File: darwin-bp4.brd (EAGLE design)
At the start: 95 x 128 mm, 21 parts, among them U1 MCP23008, U2 TCA9548A, U3 LP5012

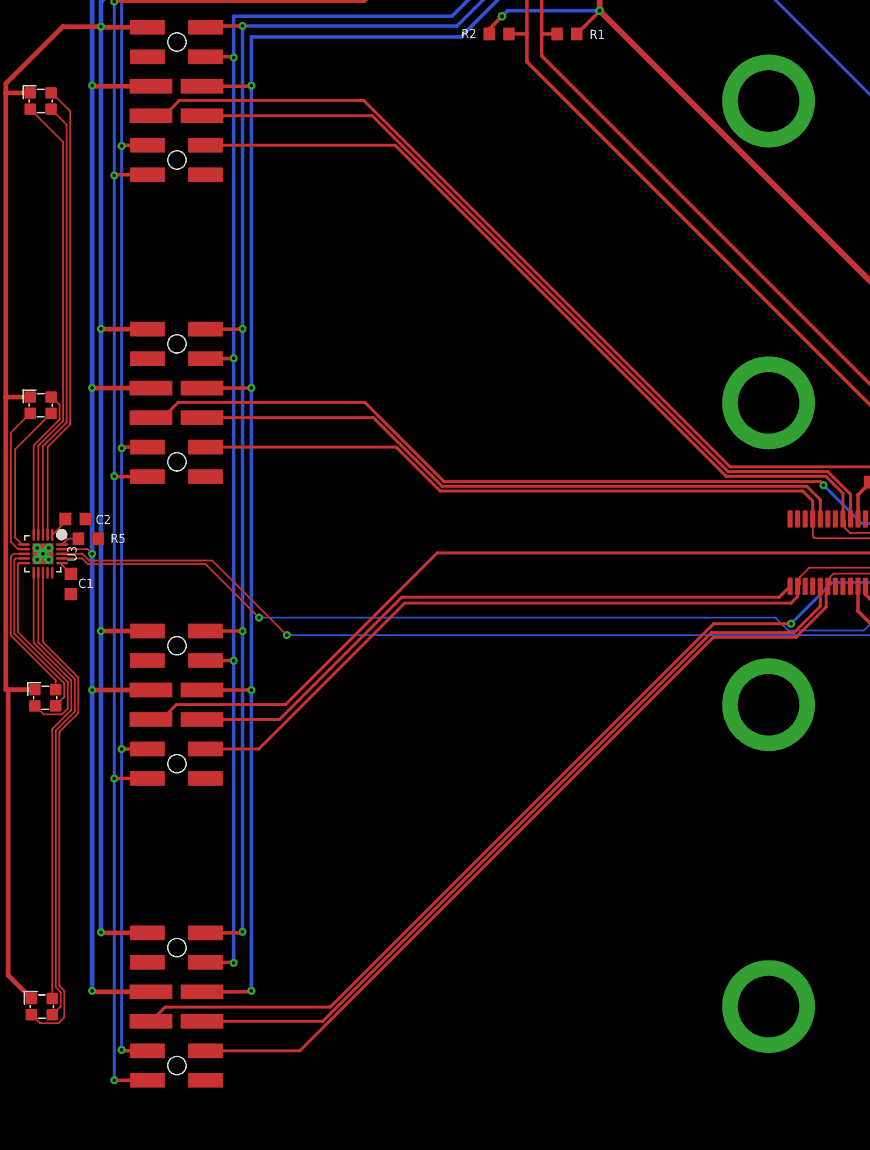
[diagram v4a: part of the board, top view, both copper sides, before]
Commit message: Fixed power to LED controller, added pulldowns on hot swap detection pins, adjusted standoff holes.
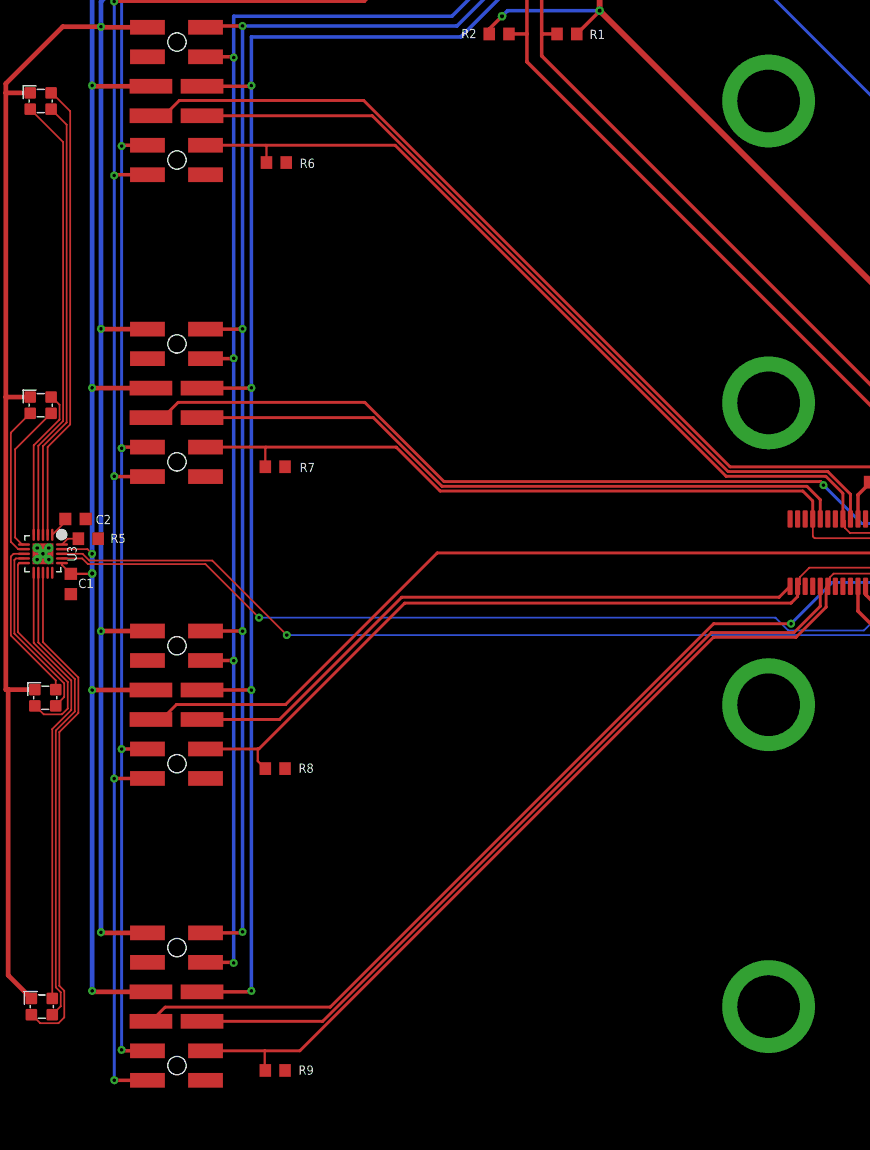
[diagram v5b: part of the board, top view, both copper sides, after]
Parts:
- added R6, R7, R8, R9: 100k, rcl:R0603
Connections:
- net GND: now also R6.2, R7.2, R8.2, R9.2
- net SC0: now also R6.1
- net SC1: now also R7.1
- net SC2: now also R8.1
- net SC3: now also R9.1
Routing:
- net SC2: track 69.5 -> 71.5 mm
- net 3V3: track 292.7 -> 294.6 mm, vias 10 -> 11
- net SC3: track 81.8 -> 83.5 mm
- net SC1: track 67.2 -> 68.9 mm
- net SC0: track 79.0 -> 80.5 mm
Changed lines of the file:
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@@
 <?xml version="1.0" encoding="utf-8"?>
 <!DOCTYPE eagle SYSTEM "eagle.dtd">
-<eagle version="9.5.0">
+<eagle version="9.5.2">
 <drawing>
 <settings>
@@
 <setting verticaltext="up"/>
 </settings>
-<grid distance="0.1" unitdist="mm" unit="mm" style="lines" multiple="1" display="yes" altdistance="0.1" altunitdist="mm" altunit="mm"/>
+<grid distance="0.5" unitdist="mm" unit="mm" style="lines" multiple="1" display="yes" altdistance="0.1" altunitdist="mm" altunit="mm"/>
 <layers>
 <layer number="1" name="Top" color="4" fill="1" visible="yes" active="yes"/>
@@
 <layer number="29" name="tStop" color="7" fill="3" visible="no" active="yes"/>
 <layer number="30" name="bStop" color="7" fill="6" visible="no" active="yes"/>
-<layer number="31" name="tCream" color="7" fill="4" visible="no" active="yes"/>
+<layer number="31" name="tCream" color="7" fill="4" visible="yes" active="yes"/>
 <layer number="32" name="bCream" color="7" fill="5" visible="no" active="yes"/>
 <layer number="33" name="tFinish" color="6" fill="3" visible="yes" active="yes"/>
@@
 <wire x1="70" y1="112.5" x2="70" y2="93.5" width="0.1524" layer="48"/>
 <hole x="67.7192" y="121.4724" drill="2.7"/>
+<wire x1="68.6" y1="106.3" x2="69.9" y2="100" width="1" layer="31" curve="-153.247402"/>
+<wire x1="68.4" y1="99.7" x2="67.1" y2="106" width="1" layer="31" curve="-153.247402"/>
+<wire x1="68.6" y1="80.3" x2="69.9" y2="74" width="1" layer="31" curve="-153.247402"/>
+<wire x1="68.4" y1="73.7" x2="67.1" y2="80" width="1" layer="31" curve="-153.247402"/>
+<wire x1="68.6" y1="54.3" x2="69.9" y2="48" width="1" layer="31" curve="-153.247402"/>
+<wire x1="68.4" y1="47.7" x2="67.1" y2="54" width="1" layer="31" curve="-153.247402"/>
+<wire x1="68.6" y1="28.3" x2="69.9" y2="22" width="1" layer="31" curve="-153.247402"/>
+<wire x1="68.4" y1="21.7" x2="67.1" y2="28" width="1" layer="31" curve="-153.247402"/>
 </plain>
 <attributes>
@@
 <element name="U$3" library="Conservify" library_urn="urn:adsk.eagle:library:11839183" package="2MMPLCC4" package3d_urn="urn:adsk.eagle:package:14540839/1" value="CLMVC-FKC-CGJJM569ABB7A343" x="6.2" y="51.6" smashed="yes" rot="R180"/>
 <element name="U$4" library="Conservify" library_urn="urn:adsk.eagle:library:11839183" package="2MMPLCC4" package3d_urn="urn:adsk.eagle:package:14540839/1" value="CLMVC-FKC-CGJJM569ABB7A343" x="5.9" y="25" smashed="yes" rot="R180"/>
+<element name="R6" library="rcl" library_urn="urn:adsk.eagle:library:334" package="R0603" package3d_urn="urn:adsk.eagle:package:23555/3" value="100k" x="26.1" y="97.7" smashed="yes">
+<attribute name="NAME" x="28.765" y="97.635" size="0.8" layer="25" rot="R180" align="center"/>
+<attribute name="SPICEPREFIX" value="R" x="26.1" y="97.7" size="0.799996875" layer="27" ratio="20" display="off"/>
+<attribute name="VALUE" x="25.465" y="95.795" size="1.27" layer="27"/>
+</element>
+<element name="R7" library="rcl" library_urn="urn:adsk.eagle:library:334" package="R0603" package3d_urn="urn:adsk.eagle:package:23555/3" value="100k" x="26" y="71.5" smashed="yes">
+<attribute name="NAME" x="28.765" y="71.435" size="0.8" layer="25" rot="R180" align="center"/>
+<attribute name="SPICEPREFIX" value="R" x="26" y="71.5" size="0.799996875" layer="27" ratio="20" display="off"/>
+<attribute name="VALUE" x="25.365" y="69.595" size="1.27" layer="27"/>
+</element>
+<element name="R8" library="rcl" library_urn="urn:adsk.eagle:library:334" package="R0603" package3d_urn="urn:adsk.eagle:package:23555/3" value="100k" x="26" y="45.5" smashed="yes">
+<attribute name="NAME" x="28.665" y="45.535" size="0.8" layer="25" rot="R180" align="center"/>
+<attribute name="SPICEPREFIX" value="R" x="26" y="45.5" size="0.799996875" layer="27" ratio="20" display="off"/>
+<attribute name="VALUE" x="25.365" y="43.595" size="1.27" layer="27"/>
+</element>
+<element name="R9" library="rcl" library_urn="urn:adsk.eagle:library:334" package="R0603" package3d_urn="urn:adsk.eagle:package:23555/3" value="100k" x="26" y="19.5" smashed="yes">
+<attribute name="NAME" x="28.665" y="19.535" size="0.8" layer="25" rot="R180" align="center"/>
+<attribute name="SPICEPREFIX" value="R" x="26" y="19.5" size="0.799996875" layer="27" ratio="20" display="off"/>
+<attribute name="VALUE" x="25.365" y="17.595" size="1.27" layer="27"/>
+</element>
 </elements>
 <signals>
@@
 <wire x1="10.234" y1="104.331" x2="10.234" y2="78.296" width="0.4064" layer="16"/>
 <wire x1="10.234" y1="78.296" x2="10.234" y2="64" width="0.4064" layer="16"/>
-<wire x1="10.234" y1="64" x2="10.234" y2="52.261" width="0.4064" layer="16"/>
+<wire x1="10.234" y1="64" x2="10.234" y2="62.3" width="0.4064" layer="16"/>
+<wire x1="10.234" y1="62.3" x2="10.234" y2="52.261" width="0.4064" layer="16"/>
 <wire x1="10.234" y1="52.261" x2="10.234" y2="26.353" width="0.4064" layer="16"/>
 <wire x1="15.3" y1="104.27" x2="10.295" y2="104.27" width="0.4064" layer="1"/>
@@
 <wire x1="79.5" y1="58.784" x2="79.708" y2="58.992" width="0.1524" layer="1"/>
 <wire x1="81" y1="57.875" x2="81" y2="58.992" width="0.1524" layer="1"/>
-<wire x1="7.6346" y1="64.4" x2="7.6346" y2="63.2" width="0" layer="19" extent="1-1"/>
+<wire x1="8.4" y1="62.275" x2="10.209" y2="62.275" width="0.2032" layer="1"/>
+<wire x1="10.209" y1="62.275" x2="10.234" y2="62.3" width="0.1524" layer="1"/>
+<via x="10.234" y="62.3" extent="1-16" drill="0.35"/>
 </signal>
 <signal name="GND">
@@
 <vertex x="0" y="0"/>
 </polygon>
-<via x="68.5" y="103" extent="1-16" drill="5.3" diameter="8"/>
-<via x="68.5" y="77" extent="1-16" drill="5.3" diameter="8"/>
-<via x="68.5" y="51" extent="1-16" drill="5.3" diameter="8"/>
-<via x="68.5" y="25" extent="1-16" drill="5.3" diameter="8"/>
+<via x="68.5" y="103" extent="1-16" drill="5.4" diameter="8"/>
+<via x="68.5" y="77" extent="1-16" drill="5.4" diameter="8"/>
+<via x="68.5" y="51" extent="1-16" drill="5.4" diameter="8"/>
+<via x="68.5" y="25" extent="1-16" drill="5.4" diameter="8"/>
 <contactref element="C2" pad="1"/>
 <contactref element="R5" pad="2"/>
@@
 <vertex x="0" y="0"/>
 </polygon>
+<contactref element="R6" pad="2"/>
+<contactref element="R7" pad="2"/>
+<contactref element="R8" pad="2"/>
+<contactref element="R9" pad="2"/>
 <wire x1="6.5" y1="64.5" x2="6" y2="64" width="0" layer="19" extent="1-1"/>
 </signal>
@@
 <contactref element="U2" pad="PIN5"/>
 <contactref element="SLOT1" pad="8"/>
-<wire x1="20" y1="99.19" x2="36.33" y2="99.19" width="0.254" layer="1"/>
+<wire x1="20" y1="99.19" x2="25.2" y2="99.19" width="0.254" layer="1"/>
+<wire x1="25.2" y1="99.19" x2="36.33" y2="99.19" width="0.254" layer="1"/>
 <wire x1="64.844" y1="70.676" x2="73.4292" y2="70.676" width="0.254" layer="1"/>
 <wire x1="74.9" y1="67" x2="74.9" y2="69.2052" width="0.254" layer="1"/>
@@
 <wire x1="78.816" y1="67.884" x2="82.176" y2="67.884" width="0.1524" layer="1"/>
 <wire x1="75.50523125" y1="65.7992" x2="77.54476875" y2="65.7992" width="0.1524" layer="1"/>
+<contactref element="R6" pad="1"/>
+<wire x1="25.25" y1="97.7" x2="25.25" y2="99.14" width="0.2" layer="1"/>
+<wire x1="25.25" y1="99.14" x2="25.2" y2="99.19" width="0.2" layer="1"/>
 </signal>
 <signal name="SC1">
 <contactref element="U2" pad="PIN9"/>
 <contactref element="SLOT2" pad="8"/>
-<wire x1="20" y1="73.19" x2="36.422" y2="73.19" width="0.254" layer="1"/>
+<wire x1="20" y1="73.19" x2="25.2" y2="73.19" width="0.254" layer="1"/>
+<wire x1="25.2" y1="73.19" x2="36.422" y2="73.19" width="0.254" layer="1"/>
 <wire x1="72.3" y1="68.554" x2="72.3" y2="67" width="0.254" layer="1"/>
 <wire x1="36.422" y1="73.19" x2="40.206" y2="69.406" width="0.254" layer="1"/>
@@
 <wire x1="72.3116" y1="65.4944" x2="72.462" y2="65.344" width="0.1524" layer="1"/>
 <wire x1="72.462" y1="65.344" x2="82.176" y2="65.344" width="0.1524" layer="1"/>
+<contactref element="R7" pad="1"/>
+<wire x1="25.15" y1="71.5" x2="25.15" y2="73.14" width="0.2" layer="1"/>
+<wire x1="25.15" y1="73.14" x2="25.2" y2="73.19" width="0.2" layer="1"/>
 </signal>
 <signal name="SD3">
@@
 <contactref element="U2" pad="PIN14"/>
 <contactref element="SLOT3" pad="8"/>
-<wire x1="20" y1="47.19" x2="24.594" y2="47.19" width="0.254" layer="1"/>
+<wire x1="20" y1="47.19" x2="24.5" y2="47.19" width="0.254" layer="1"/>
+<wire x1="24.5" y1="47.19" x2="24.594" y2="47.19" width="0.254" layer="1"/>
 <wire x1="37.158" y1="59.754" x2="70.432" y2="59.754" width="0.254" layer="1"/>
 <wire x1="70.432" y1="59.754" x2="71" y2="60.322" width="0.254" layer="1"/>
@@
 <wire x1="71.1964" y1="61.99196875" x2="72.00843125" y2="62.804" width="0.1524" layer="1"/>
 <wire x1="72.00843125" y1="62.804" x2="82.176" y2="62.804" width="0.1524" layer="1"/>
+<contactref element="R8" pad="1"/>
+<wire x1="25.15" y1="45.5" x2="24.5" y2="46.15" width="0.2" layer="1"/>
+<wire x1="24.5" y1="46.15" x2="24.5" y2="47.19" width="0.2" layer="1"/>
 </signal>
 <signal name="SD2">
@@
 <contactref element="U2" pad="PIN18"/>
 <contactref element="SLOT4" pad="8"/>
-<wire x1="20" y1="21.19" x2="28.1247375" y2="21.19" width="0.254" layer="1"/>
+<wire x1="20" y1="21.19" x2="25.1" y2="21.19" width="0.254" layer="1"/>
+<wire x1="25.1" y1="21.19" x2="28.1247375" y2="21.19" width="0.254" layer="1"/>
 <wire x1="73.4544" y1="61.0544" x2="73.6" y2="61.2" width="0.254" layer="1"/>
 <wire x1="70.8543375" y1="56.8076" x2="73.4544" y2="59.4076625" width="0.254" layer="1"/>
@@
 <wire x1="78.4076" y1="60.9224" x2="79.066" y2="60.264" width="0.1524" layer="1"/>
 <wire x1="79.066" y1="60.264" x2="82.176" y2="60.264" width="0.1524" layer="1"/>
+<contactref element="R9" pad="1"/>
+<wire x1="25.15" y1="19.5" x2="25.1" y2="19.55" width="0.2" layer="1"/>
+<wire x1="25.1" y1="19.55" x2="25.1" y2="21.19" width="0.2" layer="1"/>
 </signal>
 <signal name="SD1">

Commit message: Cleaned up schematic and added PDF.
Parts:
- C1: value .1u -> .1uf
- C2: value 1u -> 1uf
- R5: value (none) -> 4.7k
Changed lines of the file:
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@@
 <?xml version="1.0" encoding="utf-8"?>
 <!DOCTYPE eagle SYSTEM "eagle.dtd">
-<eagle version="9.5.2">
+<eagle version="9.6.1">
 <drawing>
 <settings>
@@
 </layers>
 <board>
-<fusionsync huburn="a.cGVyc29uYWw6dWUyZGRkM2Mx" projecturn="a.cGVyc29uYWw6dWUyZGRkM2MxIzIwMTgwNTA0MTMwNDQ3NTc2" f3durn="urn:adsk.wipprod:dm.lineage:7t8O2h_qR4Ken_DGyDLreg" pcbguid="e161d5e2-25b0-4dc8-b00e-eafd005bce11" lastpulledtime="" lastsyncedchangeguid="31bb6ac1-b8c7-8301-db42-d699cb3172cb"/>
+<fusionsync huburn="a.cGVyc29uYWw6dWUyZGRkM2Mx" projecturn="a.cGVyc29uYWw6dWUyZGRkM2MxIzIwMTgwNTA0MTMwNDQ3NTc2" f3durn="urn:adsk.wipprod:dm.lineage:7t8O2h_qR4Ken_DGyDLreg" pcbguid="e161d5e2-25b0-4dc8-b00e-eafd005bce11" lastpulledtime="" lastsyncedchangeguid="31bb6ac1-b8c7-8301-db42-d699cb3172cb" latestrevisionid="" lastsyncedrevisionid="" lastboardhashguid="" lastpushedtime="" linktopcb3d="%12"/>
 <plain>
 <wire x1="20.74653125" y1="116.880209375" x2="5.899615625" y2="116.882284375" width="0.1524" layer="20"/>
@@
 <attribute name="NAME" x="8.4996" y="64" size="0.8" layer="25" ratio="20" rot="R270" align="center"/>
 </element>
-<element name="C1" library="rcl" library_urn="urn:adsk.eagle:library:334" package="C0603K" package3d_urn="urn:adsk.eagle:package:23680/2" value=".1u" x="8.4" y="61.4" smashed="yes" rot="R90">
+<element name="C1" library="rcl" library_urn="urn:adsk.eagle:library:334" package="C0603K" package3d_urn="urn:adsk.eagle:package:23680/2" value=".1uf" x="8.4" y="61.4" smashed="yes" rot="R90">
 <attribute name="NAME" x="9.7" y="61.45" size="0.8" layer="25" ratio="20" rot="R180" align="center"/>
 <attribute name="POPULARITY" value="30" x="8.4" y="61.4" size="1.778" layer="27" rot="R90" display="off"/>
 <attribute name="SPICEPREFIX" value="C" x="8.4" y="61.4" size="1.778" layer="27" rot="R90" display="off"/>
 </element>
-<element name="C2" library="rcl" library_urn="urn:adsk.eagle:library:334" package="C0603K" package3d_urn="urn:adsk.eagle:package:23680/2" value="1u" x="8.8" y="67" smashed="yes" rot="R180">
+<element name="C2" library="rcl" library_urn="urn:adsk.eagle:library:334" package="C0603K" package3d_urn="urn:adsk.eagle:package:23680/2" value="1uf" x="8.8" y="67" smashed="yes" rot="R180">
 <attribute name="NAME" x="11.2" y="66.95" size="0.8" layer="25" ratio="20" rot="R180" align="center"/>
 <attribute name="POPULARITY" value="30" x="8.8" y="67" size="1.778" layer="27" rot="R180" display="off"/>
 <attribute name="SPICEPREFIX" value="C" x="8.8" y="67" size="1.778" layer="27" rot="R180" display="off"/>
 </element>
-<element name="R5" library="rcl" library_urn="urn:adsk.eagle:library:334" package="R0603" package3d_urn="urn:adsk.eagle:package:23555/3" value="" x="9.9" y="65.3" smashed="yes">
+<element name="R5" library="rcl" library_urn="urn:adsk.eagle:library:334" package="R0603" package3d_urn="urn:adsk.eagle:package:23555/3" value="4.7k" x="9.9" y="65.3" smashed="yes">
 <attribute name="NAME" x="12.465" y="65.335" size="0.8" layer="25" ratio="20" align="center"/>
 <attribute name="SPICEPREFIX" value="R" x="9.9" y="65.3" size="1.778" layer="27" display="off"/>
@@
 <contactref element="SLOT3" pad="2"/>
 <contactref element="SLOT4" pad="2"/>
-<contactref element="U2" pad="PIN12"/>
 <contactref element="U1" pad="3"/>
 <contactref element="U1" pad="4"/>
@@
 <contactref element="R8" pad="2"/>
 <contactref element="R9" pad="2"/>
-<wire x1="6.5" y1="64.5" x2="6" y2="64" width="0" layer="19" extent="1-1"/>
+<contactref element="U2" pad="PIN12"/>
+<wire x1="68.5" y1="77" x2="68.5" y2="103" width="0" layer="19" extent="1-1"/>
+<wire x1="70.35" y1="67" x2="68.5" y2="77" width="0" layer="19" extent="1-1"/>
+<wire x1="76.85" y1="67" x2="70.35" y2="67" width="0" layer="19" extent="1-1"/>
+<wire x1="77.5" y1="67" x2="76.85" y2="67" width="0" layer="19" extent="1-1"/>
+<wire x1="75.55" y1="61.2" x2="76.85" y2="67" width="0" layer="19" extent="1-1"/>
+<wire x1="79.5" y1="56.125" x2="75.55" y2="61.2" width="0" layer="19" extent="1-1"/>
+<wire x1="81" y1="56.125" x2="79.5" y2="56.125" width="0" layer="19" extent="1-1"/>
+<wire x1="91.4832" y1="61.534" x2="81" y2="56.125" width="0" layer="19" extent="1-1"/>
+<wire x1="91.4832" y1="62.804" x2="91.4832" y2="61.534" width="0" layer="19" extent="1-1"/>
+<wire x1="91.4832" y1="64.074" x2="91.4832" y2="62.804" width="0" layer="19" extent="1-1"/>
+<wire x1="91.4832" y1="69.154" x2="91.4832" y2="64.074" width="0" layer="19" extent="1-1"/>
+<wire x1="68.5" y1="51" x2="79.5" y2="56.125" width="0" layer="19" extent="1-1"/>
+<wire x1="68.5" y1="25" x2="68.5" y2="51" width="0" layer="19" extent="1-1"/>
+<wire x1="42.6042" y1="121.68" x2="68.5" y2="103" width="0" layer="19" extent="1-1"/>
+<wire x1="41.3342" y1="121.68" x2="42.6042" y2="121.68" width="0" layer="19" extent="1-1"/>
+<wire x1="26.95" y1="97.7" x2="41.3342" y2="121.68" width="0" layer="19" extent="1-1"/>
+<wire x1="15" y1="106.81" x2="26.95" y2="97.7" width="0" layer="19" extent="1-1"/>
+<wire x1="15" y1="80.81" x2="26.95" y2="97.7" width="0" layer="19" extent="1-1"/>
+<wire x1="9.675" y1="67" x2="15" y2="80.81" width="0" layer="19" extent="1-1"/>
+<wire x1="10.75" y1="65.3" x2="9.675" y2="67" width="0" layer="19" extent="1-1"/>
+<wire x1="6.5" y1="64.5" x2="9.675" y2="67" width="0" layer="19" extent="1-1"/>
+<wire x1="6" y1="64" x2="6.5" y2="64.5" width="0" layer="19" extent="1-1"/>
+<wire x1="5.5" y1="64.5" x2="6" y2="64" width="0" layer="19" extent="1-1"/>
+<wire x1="6.5" y1="63.5" x2="6" y2="64" width="0" layer="19" extent="1-1"/>
+<wire x1="5.5" y1="63.5" x2="6" y2="64" width="0" layer="19" extent="1-1"/>
+<wire x1="6.4" y1="62.3654" x2="6.5" y2="63.5" width="0" layer="19" extent="1-1"/>
+<wire x1="6.8" y1="62.3654" x2="6.4" y2="62.3654" width="0" layer="19" extent="1-1"/>
+<wire x1="8.4" y1="60.525" x2="6.8" y2="62.3654" width="0" layer="19" extent="1-1"/>
+<wire x1="15" y1="54.81" x2="8.4" y2="60.525" width="0" layer="19" extent="1-1"/>
+<wire x1="26.85" y1="71.5" x2="15" y2="80.81" width="0" layer="19" extent="1-1"/>
+<wire x1="26.85" y1="45.5" x2="15" y2="54.81" width="0" layer="19" extent="1-1"/>
+<wire x1="15" y1="28.81" x2="26.85" y2="45.5" width="0" layer="19" extent="1-1"/>
+<wire x1="26.85" y1="19.5" x2="15" y2="28.81" width="0" layer="19" extent="1-1"/>
 </signal>
 <signal name="N$10">
